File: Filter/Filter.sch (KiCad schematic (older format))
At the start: 69 parts, among them J1 Conn_Coaxial, J10 Conn_01x02, J11 Conn_01x08, J2 Conn_01x02, J3 Conn_Coaxial, J4 Conn_01x02, J5 Conn_01x02, J6 Conn_01x01, J7 Conn_01x01, J8 Conn_01x01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

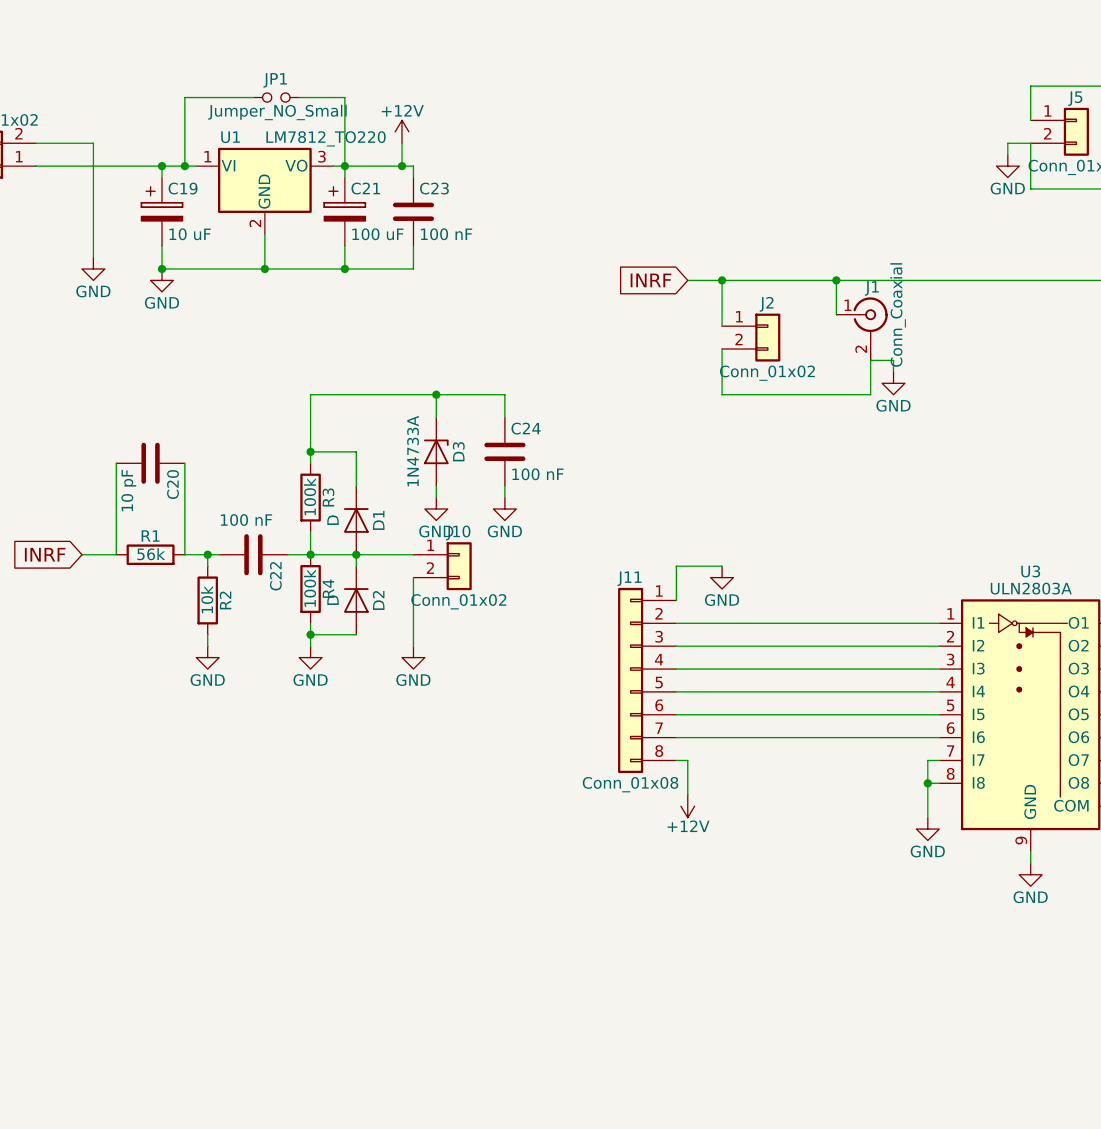
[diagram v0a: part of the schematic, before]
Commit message: Added some extra protection and fixed labels on Filter
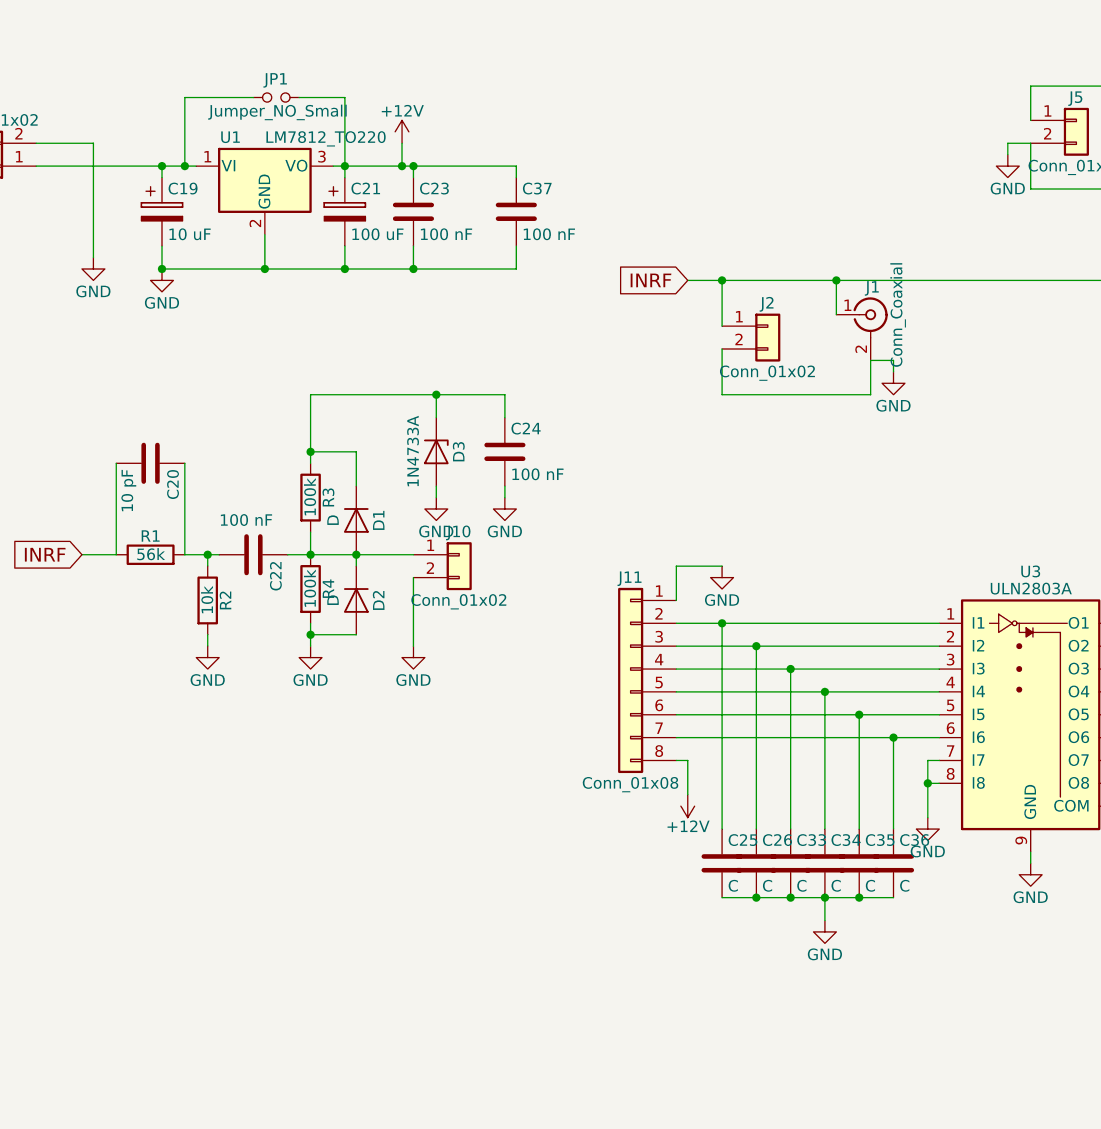
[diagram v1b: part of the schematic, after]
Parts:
- added C25, C26, C33, C34, C35, C36: C, Capacitors_THT:C_Disc_D5.0mm_W2.5mm_P2.50mm, symbol C
- added C37: 100 nF, Capacitors_THT:C_Disc_D5.0mm_W2.5mm_P2.50mm, symbol C
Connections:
- net +12V: now also C37.1
- net GND: now also C25.2, C26.2, C33.2, C34.2, C35.2, C36.2, C37.2
- net at J11.2 (Pin_2), U3.1 (I1): now also C25.1
- net at J11.3 (Pin_3), U3.2 (I2): now also C26.1
- net at J11.4 (Pin_4), U3.3 (I3): now also C33.1
- net at J11.5 (Pin_5), U3.4 (I4): now also C34.1
- net at J11.6 (Pin_6), U3.5 (I5): now also C35.1
- net at J11.7 (Pin_7), U3.6 (I6): now also C36.1

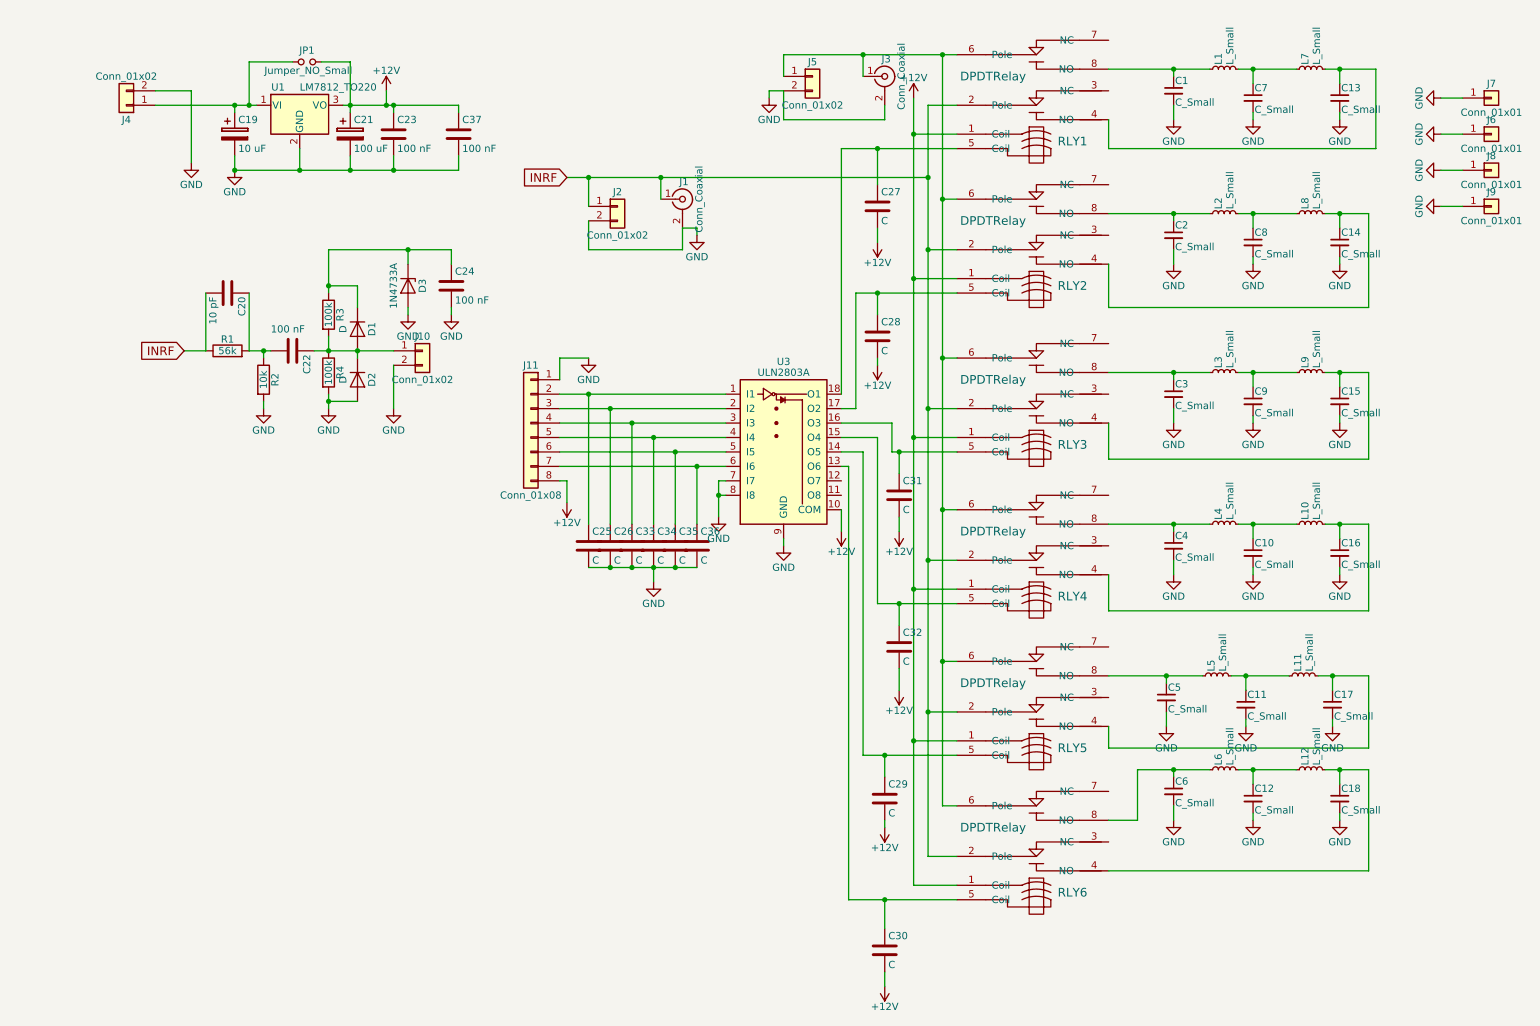
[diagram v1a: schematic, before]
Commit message: Added tandem match to sense power to filter board
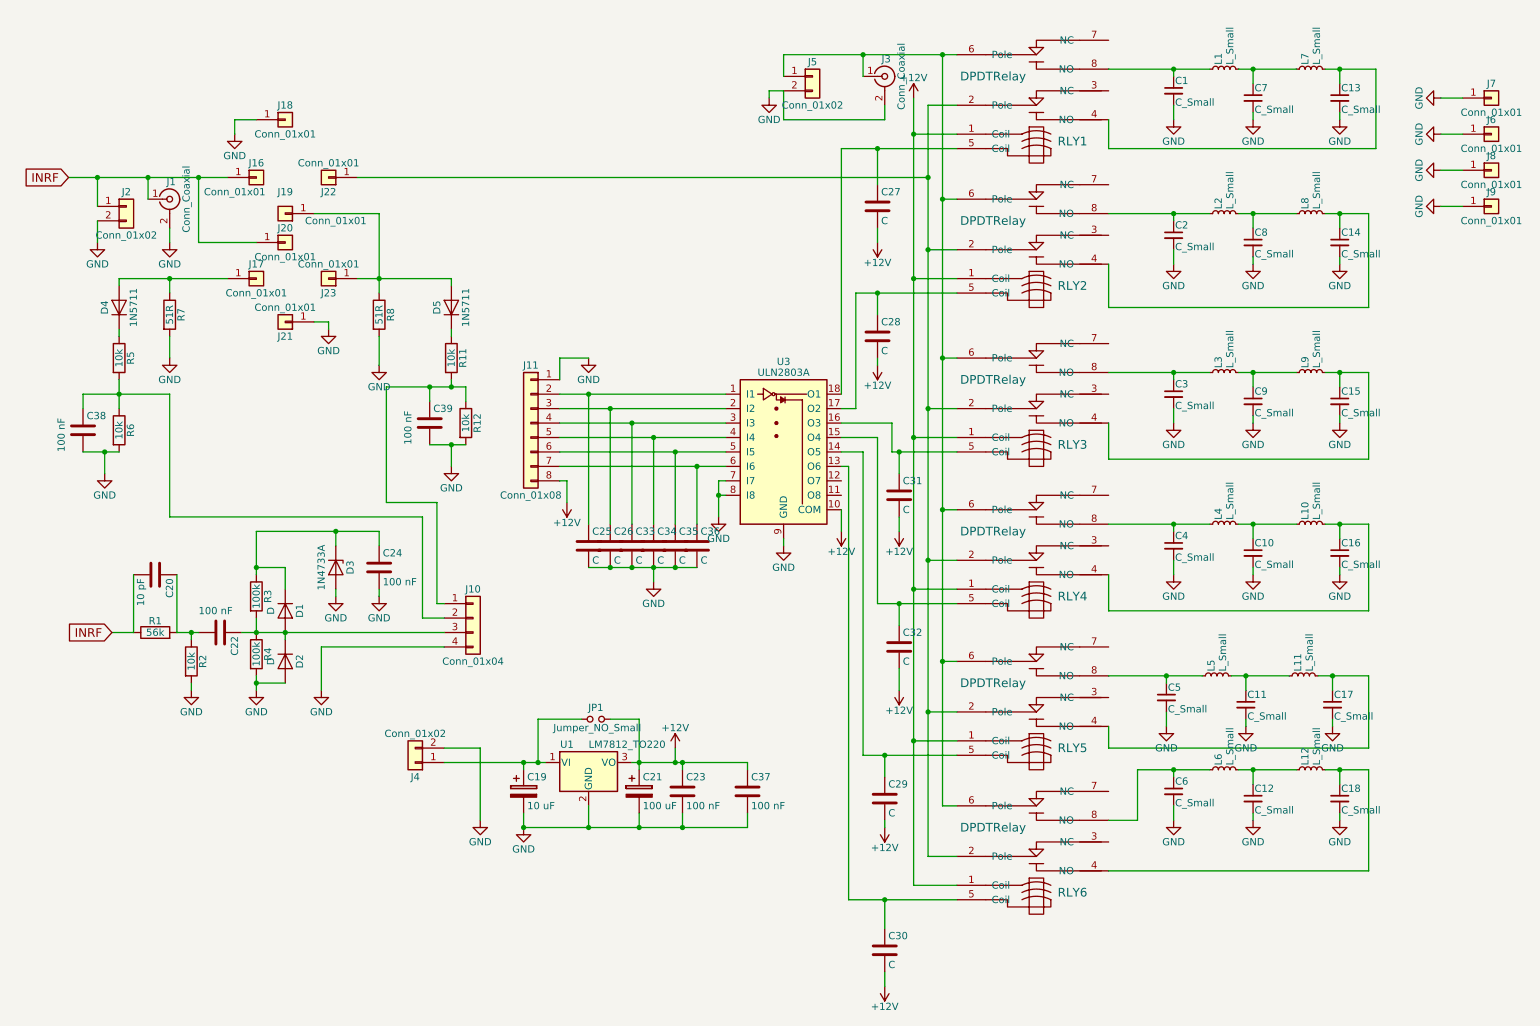
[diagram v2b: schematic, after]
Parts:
- removed J10: Conn_01x02, Connectors_Terminal_Blocks:TerminalBlock_bornier-2_P5.08mm, symbol Conn_01x02
- added C38, C39: 100 nF, Capacitors_THT:C_Disc_D5.0mm_W2.5mm_P2.50mm, symbol C
- added D4, D5: 1N5711, Diodes_THT:D_DO-35_SOD27_P7.62mm_Horizontal, symbol D
- added J10: Conn_01x04, Connectors_Molex:Molex_KK-6410-04_04x2.54mm_Straight, symbol Conn_01x04
- added J16, J17, J18, J19, J20, J21, J22, J23: Conn_01x01, Connectors:1pin, symbol Conn_01x01
- added R11, R12, R5, R6: 10k, Resistors_THT:R_Axial_DIN0207_L6.3mm_D2.5mm_P7.62mm_Horizontal, symbol R
- added R7, R8: 51R, Resistors_THT:R_Axial_DIN0309_L9.0mm_D3.2mm_P12.70mm_Horizontal, symbol R
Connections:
- net GND: now also C38.2, C39.2, J10.4 (Pin_4), J18.1 (Pin_1), J21.1 (Pin_1), R12.2, R6.2, R7.2, R8.2
- net INRF: now also J16.1 (Pin_1), J20.1 (Pin_1); no longer RLY1.2 (Pole), RLY2.2 (Pole), RLY3.2 (Pole), RLY4.2 (Pole), RLY5.2 (Pole), RLY6.2 (Pole)
- net at C22.1, D1.2 (A), D2.1 (K)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: now also J10.3 (Pin_3)
- new net: J22.1 (Pin_1), RLY1.2 (Pole), RLY2.2 (Pole), RLY3.2 (Pole), RLY4.2 (Pole), RLY5.2 (Pole), RLY6.2 (Pole)
- new net: C39.1, J10.1 (Pin_1), R11.2, R12.1
- new net: C38.1, J10.2 (Pin_2), R5.2, R6.1
- new net: D4.2 (A), J17.1 (Pin_1), R7.1
- new net: D5.2 (A), J19.1 (Pin_1), J23.1 (Pin_1), R8.1
- new net: D4.1 (K), R5.1
- new net: D5.1 (K), R11.1
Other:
- moved on the sheet: C19, C20, C21, C22, C23, C24, C37, D1, D2, D3, J1, J2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

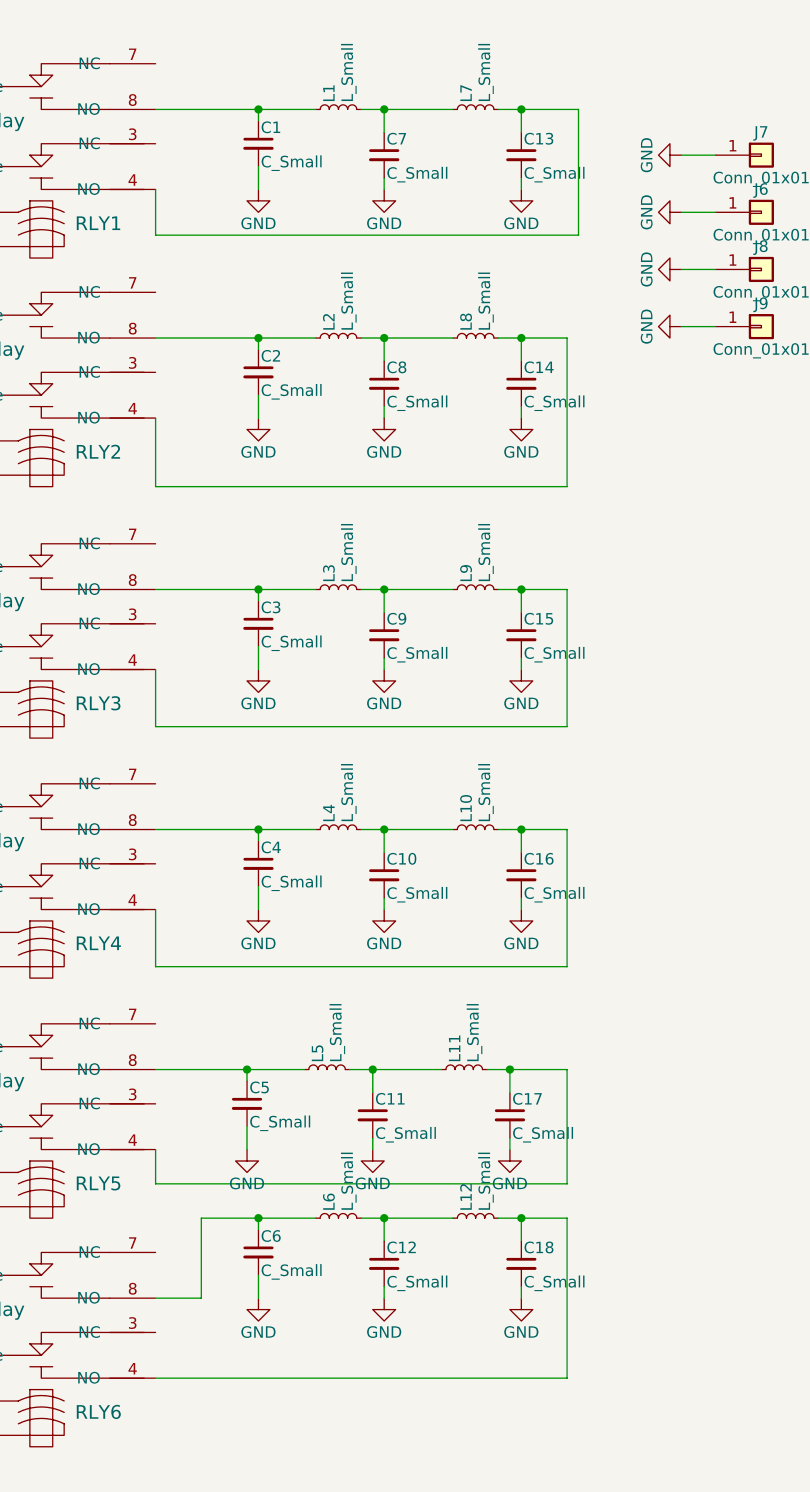
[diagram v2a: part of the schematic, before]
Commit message: Moved series resistor closer to common drain amplifier to prevent oscillation
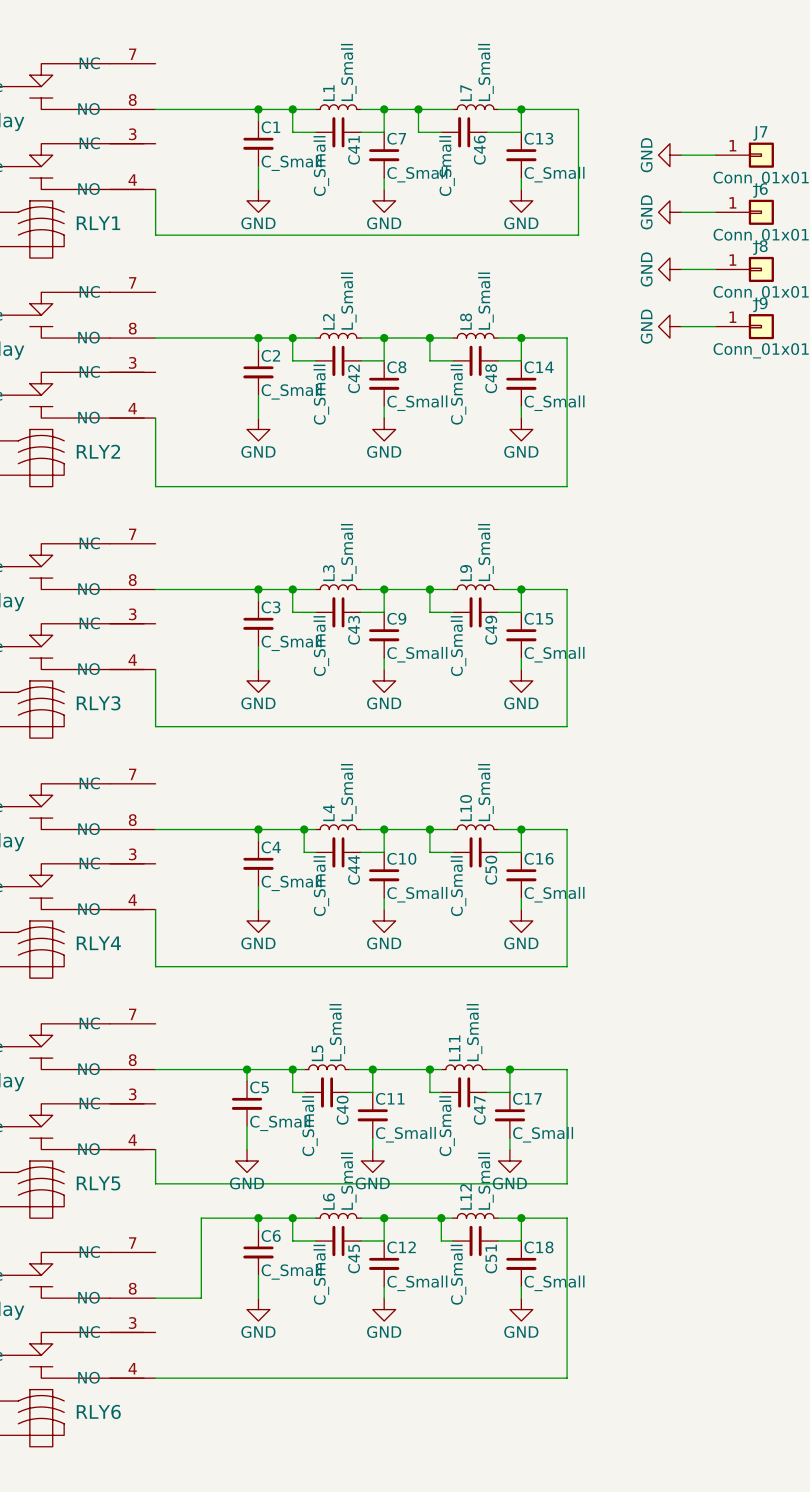
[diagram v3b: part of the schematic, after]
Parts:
- added C40, C41, C42, C43, C44, C45, C46, C47, C48, C49, C50, C51: C_Small, FilterD:C_Disc_SMD, symbol C_Small
- L1, L10, L11, L12, L2, L3, L4, L5, L6, L7, L8, L9: footprint Inductors_THT:L_Toroid_Vertical_L13.0mm_W6.5mm_P5.60mm -> FilterD:L_Toroid_Vertical_L13.0mm_W6.5mm_P5.60mm_mod
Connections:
- net at C1.1, L1.1, RLY1.8 (NO): now also C41.2
- net at C7.1, L1.2, L7.1: now also C41.1, C46.2
- net at C13.1, L7.2, RLY1.4 (NO): now also C46.1
- net at C2.1, L2.1, RLY2.8 (NO): now also C42.2
- net at C8.1, L2.2, L8.1: now also C42.1, C48.2
- net at C14.1, L8.2, RLY2.4 (NO): now also C48.1
- net at C3.1, L3.1, RLY3.8 (NO): now also C43.2
- net at C9.1, L3.2, L9.1: now also C43.1, C49.2
- net at C15.1, L9.2, RLY3.4 (NO): now also C49.1
- net at C4.1, L4.1, RLY4.8 (NO): now also C44.2
- net at C10.1, L10.1, L4.2: now also C44.1, C50.2
- net at C16.1, L10.2, RLY4.4 (NO): now also C50.1
- net at C5.1, L5.1, RLY5.8 (NO): now also C40.2
- net at C11.1, L11.1, L5.2: now also C40.1, C47.2
- net at C17.1, L11.2, RLY5.4 (NO): now also C47.1
- net at C6.1, L6.1, RLY6.8 (NO): now also C45.2
- net at C12.1, L12.1, L6.2: now also C45.1, C51.2
- net at C18.1, L12.2, RLY6.4 (NO): now also C51.1
